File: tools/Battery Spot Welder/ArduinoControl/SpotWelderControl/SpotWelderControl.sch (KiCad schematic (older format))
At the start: 11 parts, among them J1 12v Power, J2 RELAY, J3 AudioJack2_Switch

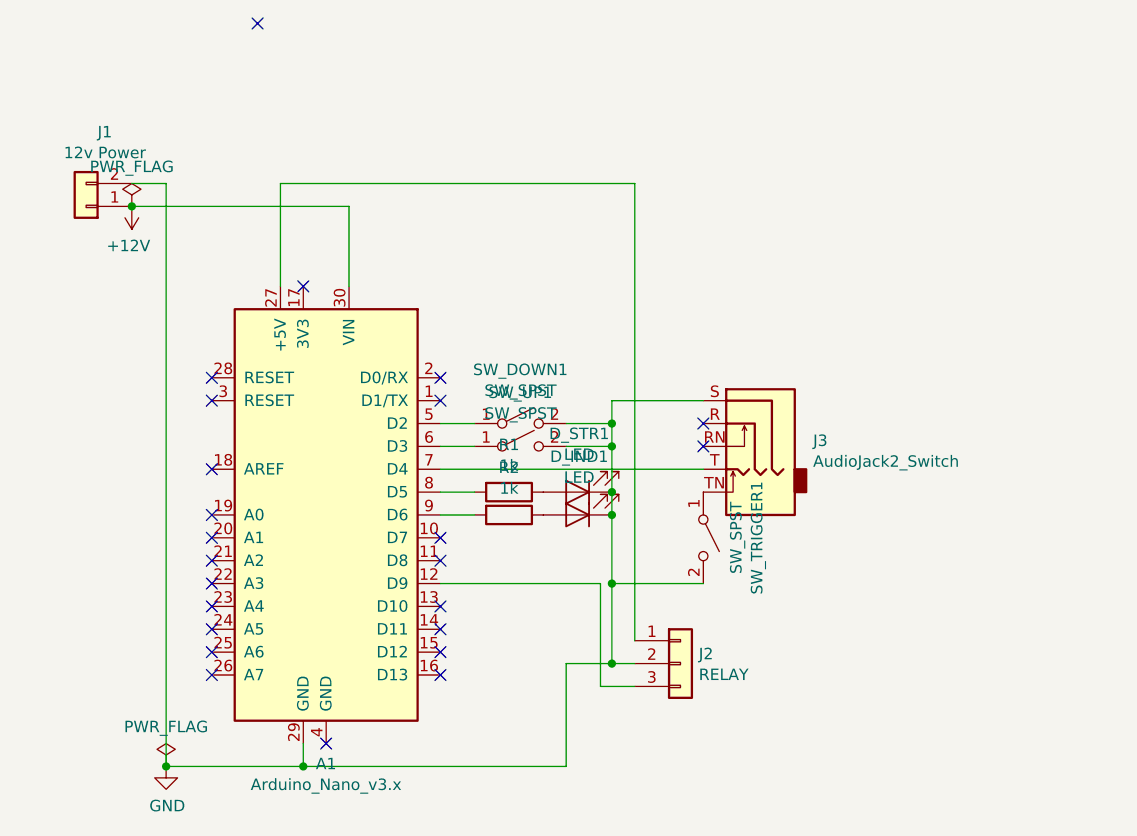
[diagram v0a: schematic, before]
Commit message: Added a large capacitor to the arduino controller. Should keep voltage drop during the pulse to a minimum, and allow the controller to keep running. Added the panel buttons and relay standoff supports.
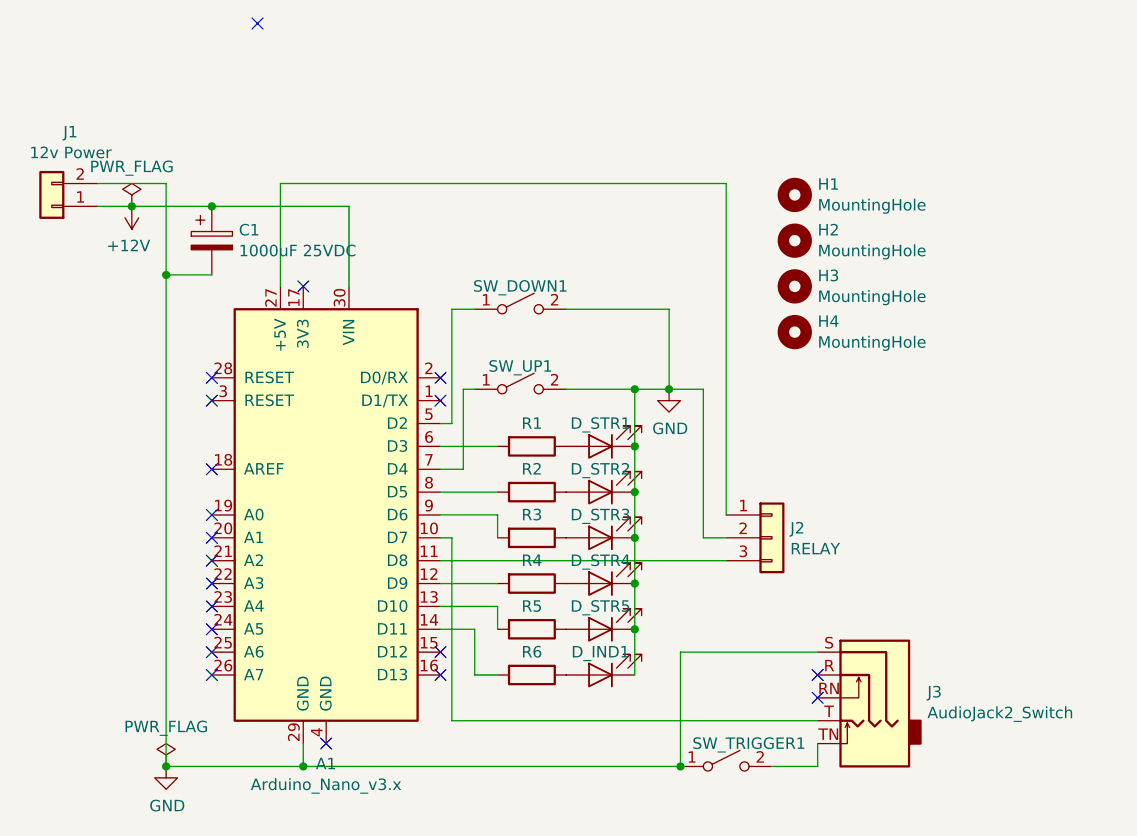
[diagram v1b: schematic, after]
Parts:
- added C1: 1000uF 25VDC, Capacitor_THT:CP_Radial_D10.0mm_P5.00mm_P7.50mm, symbol Device:CP
- added D_IND1, D_STR3, D_STR4, D_STR5: LED, LED_THT:LED_D3.0mm, symbol Device:LED
- added H1, H2, H3, H4: MountingHole, MountingHole:MountingHole_3.2mm_M3_DIN965_Pad, symbol Mechanical:MountingHole
- added R3, R4, R5, R6: 1k, Resistor_THT:R_Axial_DIN0207_L6.3mm_D2.5mm_P7.62mm_Horizontal, symbol Device:R
- J1: footprint Connector_PinHeader_2.54mm:PinHeader_1x02_P2.54mm_Vertical -> Connector_JST:JST_XH_B2B-XH-A_1x02_P2.50mm_Vertical
- renumbered D_IND1 to D_STR2
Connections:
- net +12V: now also C1.1
- net GND: now also SW_TRIGGER1.1 (A), C1.2, D_IND1.1 (K), D_STR3.1 (K), D_STR4.1 (K), D_STR5.1 (K); no longer SW_TRIGGER1.2 (B)
- net at J3.TN: now also SW_TRIGGER1.2 (B); no longer SW_TRIGGER1.1 (A)
- net at SW_UP1.1 (A): now also A1.7 (D4); no longer A1.6 (D3)
- net at R2.2: now also A1.8 (D5); no longer A1.9 (D6)
- net at R1.2: now also A1.6 (D3); no longer A1.8 (D5)
- net at J3.T: now also A1.10 (D7); no longer A1.7 (D4)
- net at A1.11 (D8): now also J2.3 (Pin_3)
- net at A1.12 (D9): now also R4.2; no longer J2.3 (Pin_3)
- net at A1.13 (D10): now also R5.2
- net at A1.14 (D11): now also R6.2
- new net: A1.9 (D6), R3.2
- new net: D_STR3.2 (A), R3.1
- new net: D_STR4.2 (A), R4.1
- new net: D_STR5.2 (A), R5.1
- new net: D_IND1.2 (A), R6.1
- no-connect marks 24 -> 20
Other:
- moved on the sheet: D_STR1, D_STR2, J1, J2, J3, R1, R2, SW_DOWN1, SW_TRIGGER1, SW_UP1
